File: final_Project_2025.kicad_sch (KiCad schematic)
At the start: 20 parts, among them J1 Conn_02x16_Top_Bottom, Q1 TIP42C, Q2 2N2219, Q3 2N2219, Q4 TIP42C, U1 DRV8833PWP, U2 DRV8833PWP, U3 INA219AxD

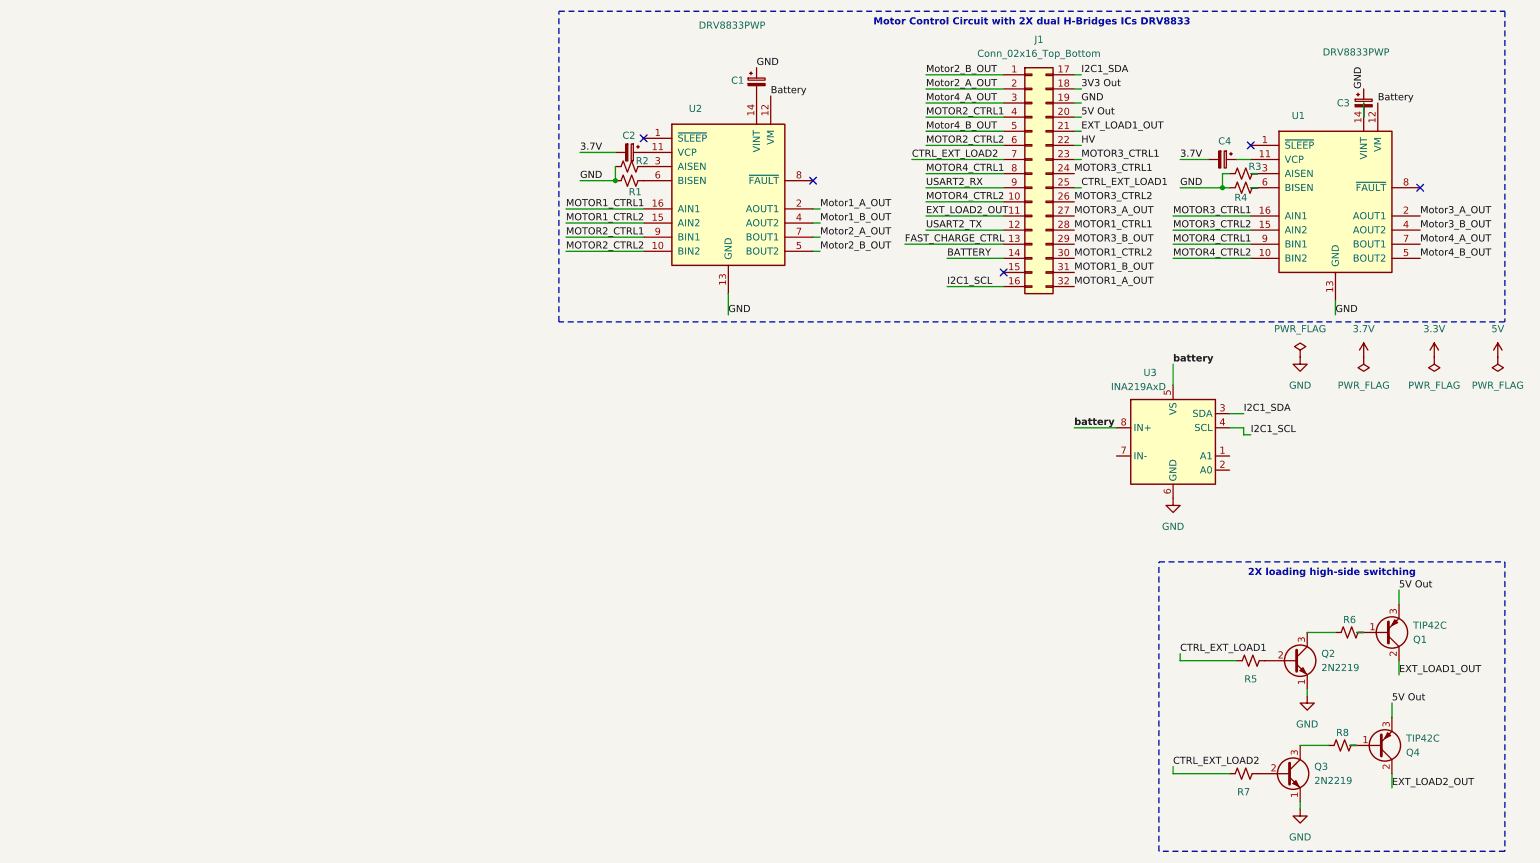
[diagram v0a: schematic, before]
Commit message: added ch224k to schematic
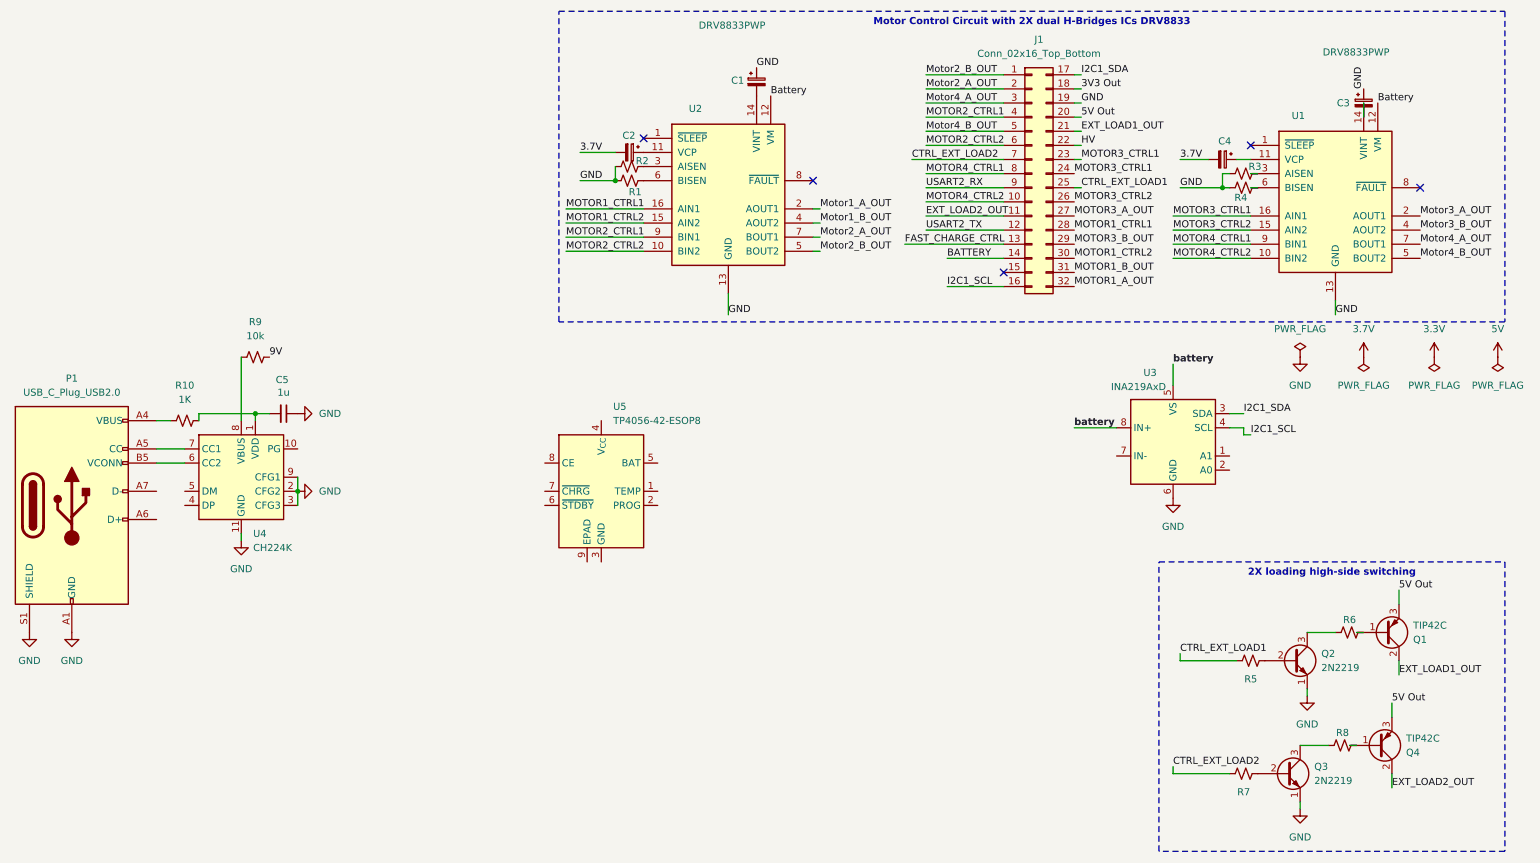
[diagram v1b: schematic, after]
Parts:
- added C5: 1u, symbol Device:C_Small
- added P1: USB_C_Plug_USB2.0, symbol Connector:USB_C_Plug_USB2.0
- added R10: 1K, symbol Device:R_Small_US
- added R9: 10k, symbol Device:R_Small_US
- added U4: CH224K, Package_SO:SSOP-10-1EP_3.9x4.9mm_P1mm_EP2.1x3.3mm, symbol Interface_USB:CH224K
- added U5: TP4056-42-ESOP8, Package_SO:SOIC-8-1EP_3.9x4.9mm_P1.27mm_EP2.41x3.3mm_ThermalVias, symbol Battery_Management:TP4056-42-ESOP8
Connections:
- net GND: now also C5.1, P1.A1 (GND), P1.A12 (GND), P1.B1 (GND), P1.B12 (GND), P1.S1 (SHIELD), U4.11 (GND), U4.2 (CFG2), U4.3 (CFG3), U4.9 (CFG1)
- new net: P1.A4 (VBUS), P1.A9 (VBUS), P1.B4 (VBUS), P1.B9 (VBUS), R10.1
- new net: C5.2, R10.2, U4.1 (VDD)
- new net: P1.B5 (VCONN), U4.6 (CC2)
- new net: P1.A5 (CC), U4.7 (CC1)
- new net: R9.1, U4.8 (VBUS)
- new net 9V: R9.2
